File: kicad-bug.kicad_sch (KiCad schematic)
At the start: 2 parts

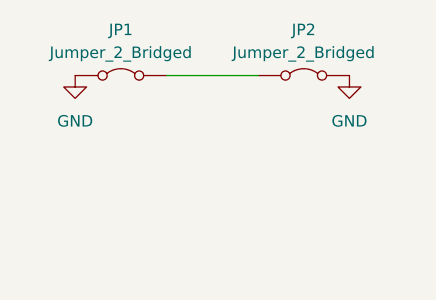
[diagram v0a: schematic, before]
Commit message: after poking around with filling zones and running DRC
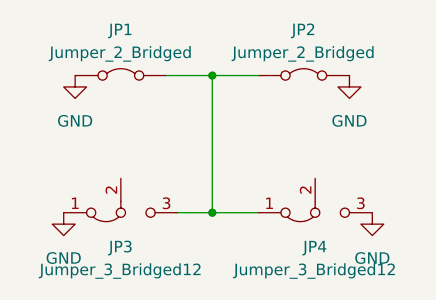
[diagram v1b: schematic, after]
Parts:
- added JP3, JP4: Jumper_3_Bridged12, Jumper:SolderJumper-3_P1.3mm_Bridged12_RoundedPad1.0x1.5mm, symbol Jumper:Jumper_3_Bridged12
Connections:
- net GND: now also JP3.1 (A), JP4.3 (B)
- net at JP1.2 (B), JP2.1 (A): now also JP3.3 (B), JP4.1 (A)
